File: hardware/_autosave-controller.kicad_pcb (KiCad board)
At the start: 4 copper layers, 32 x 93.3 mm, 38 parts, among them J1 Connector, USB-TYPE-C-16P, J2 AXK6F20347YG, J3 AFA01-S08FCA-00, U1 ESP32-C6-WROOM-1, U2 BQ24074RGTR, U3 TLA2518IRTER, U6 TPS62142RGTR

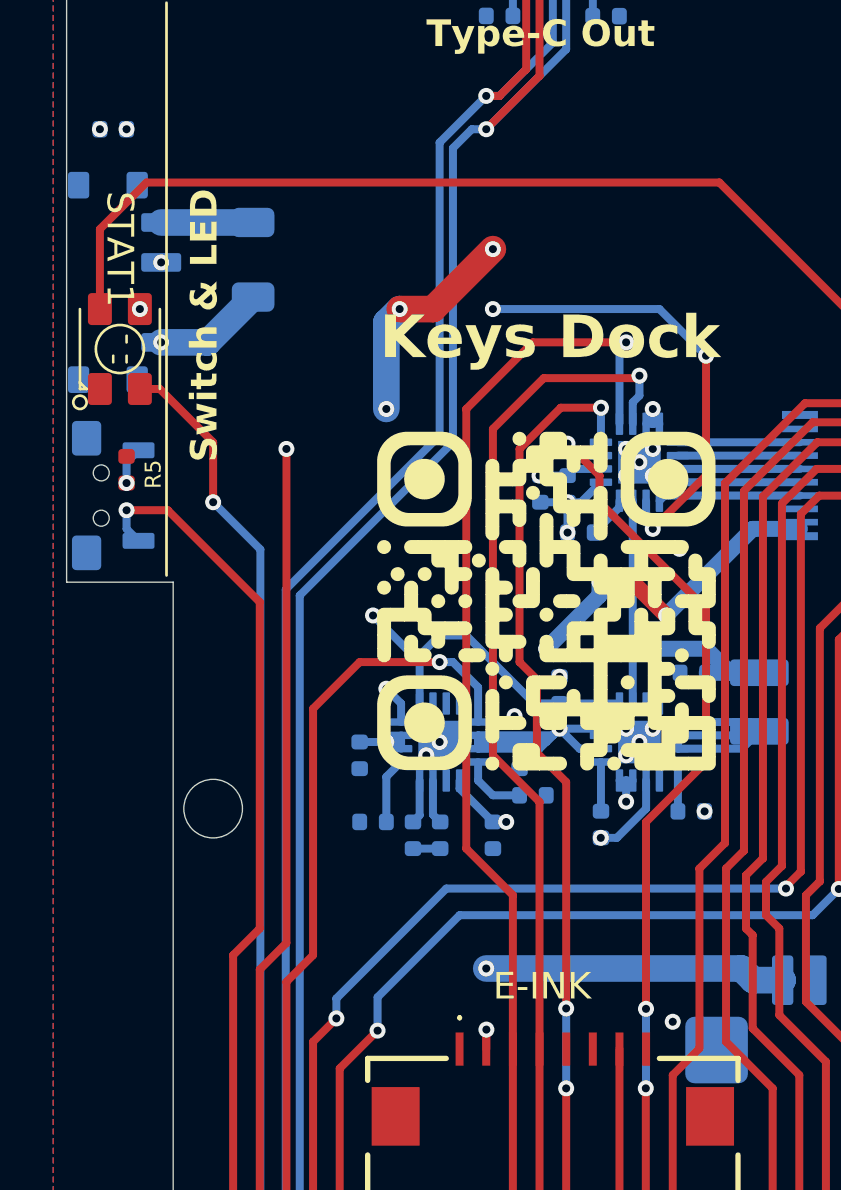
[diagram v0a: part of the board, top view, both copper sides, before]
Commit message: :sparkles: use side reset button
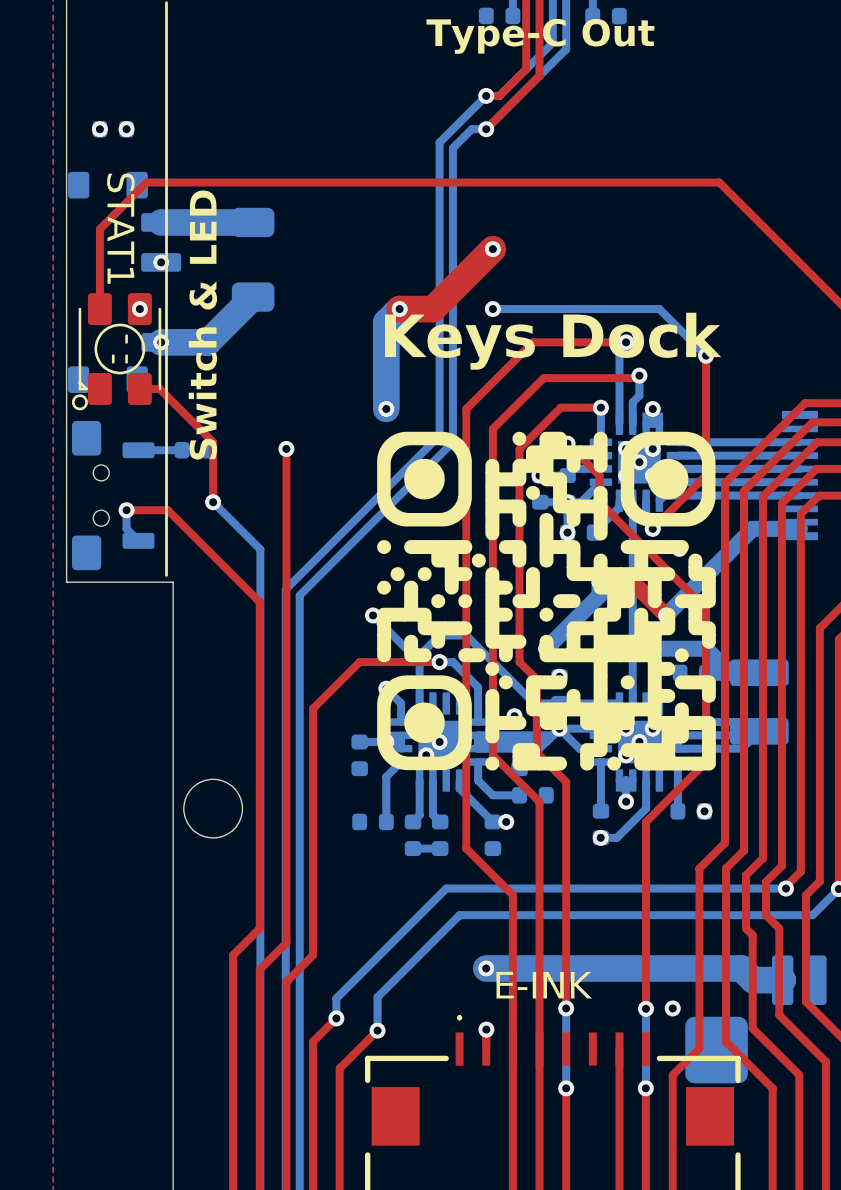
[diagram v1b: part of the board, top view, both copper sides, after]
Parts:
- R5: moved to B.Cu
- moved R5 2.68 mm to (77.8, 75.5), turned to 0 degrees
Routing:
- net Net-(S1-A): track 1.42 -> 1.63 mm, vias 1 -> 0
